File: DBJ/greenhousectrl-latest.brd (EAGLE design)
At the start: 69.5 x 80 mm, 54 parts, among them IC1 ATMEGA168TQFP-08, IC4 L298, J1 5.5x2.1mm Barrel, K1 RELAYPTH4, Q1 MMBT2222A, U2 V_REG_317SMD, Y2 16MHZ

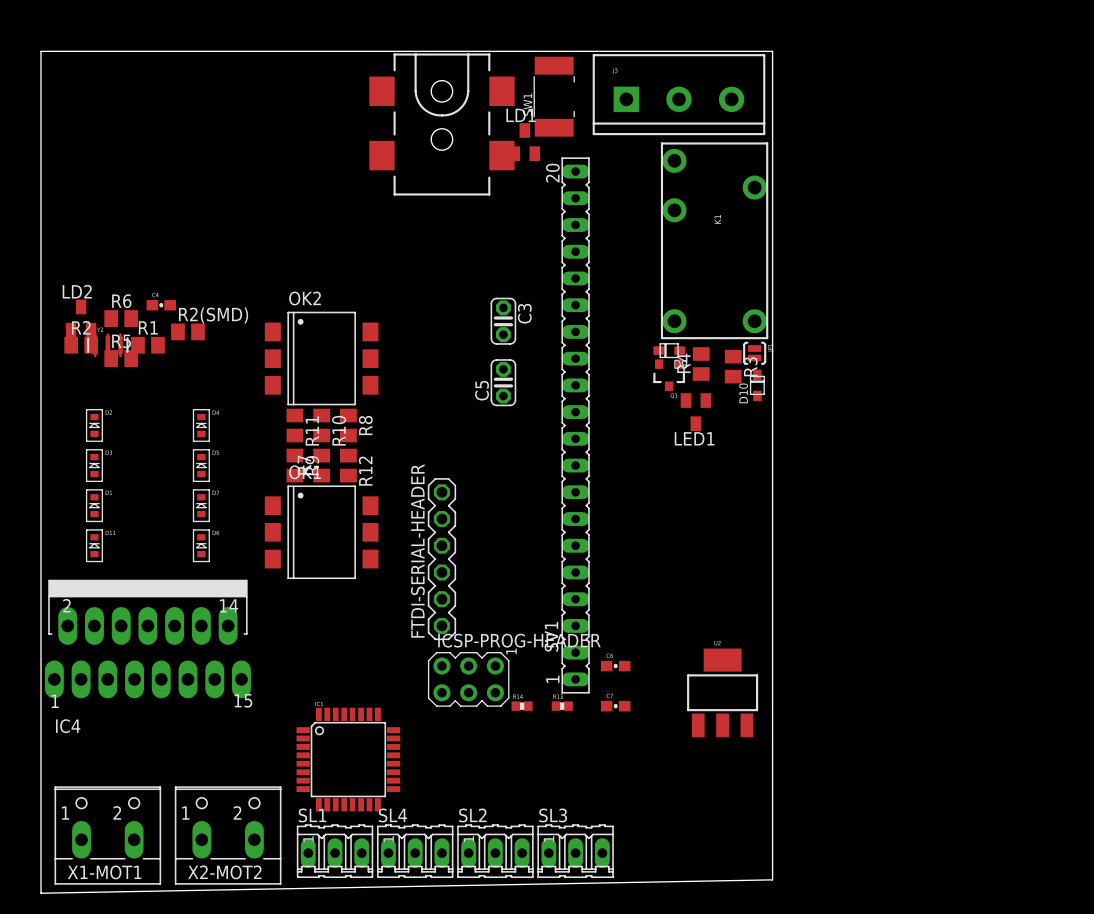
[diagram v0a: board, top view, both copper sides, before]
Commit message: Updated Schematic
clearly shows subsystems for pcb layout
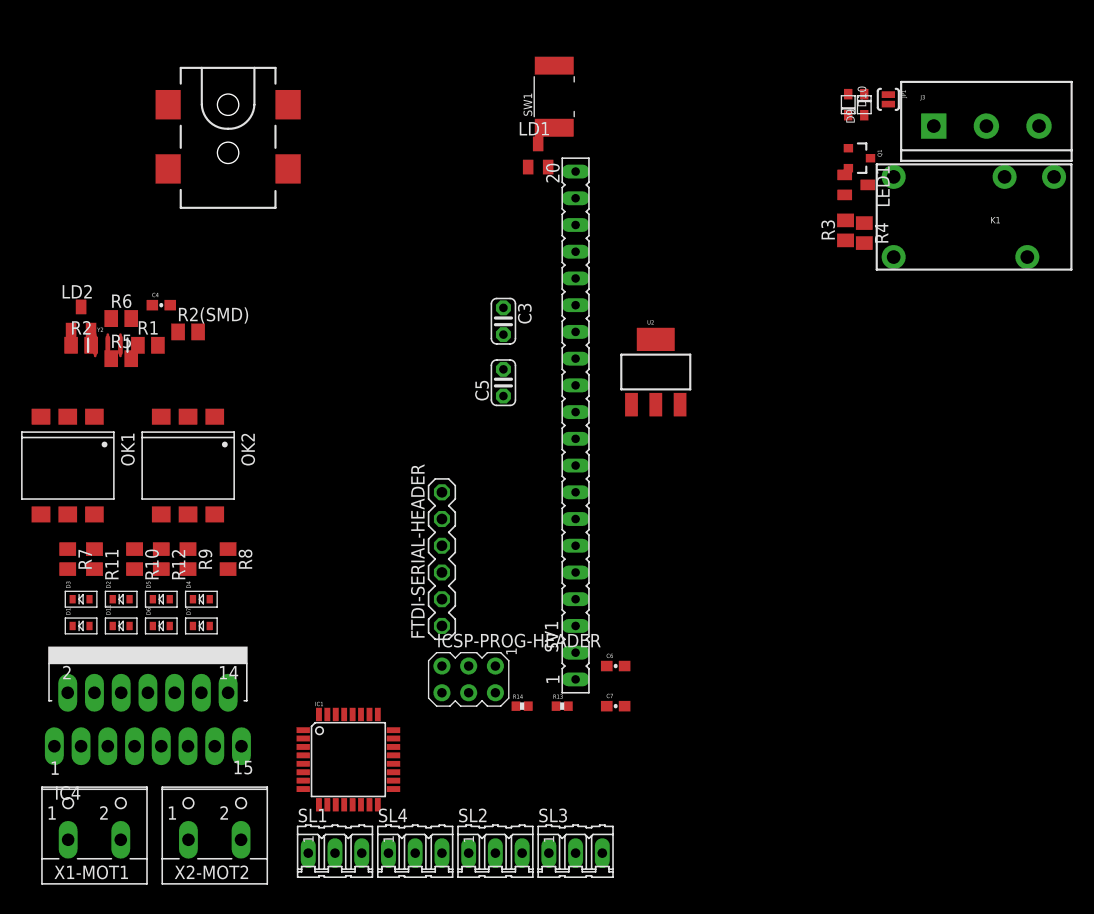
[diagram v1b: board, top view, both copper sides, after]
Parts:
- moved U2 31.1 mm to (58.4, 49.5)
- moved D9 29.8 mm to (78.2, 74.9), turned to 90 degrees
- moved J3 29.3 mm to (84.8, 72.9)
- moved D10 28.0 mm to (76.7, 74.9), turned to 270 degrees
- moved Q1 27.4 mm to (77.7, 69.8), turned to 270 degrees
- moved JP1 27.3 mm to (80.5, 75.4)
- moved LED1 26.4 mm to (77.5, 67.3), turned to 270 degrees
- moved K1 25.9 mm to (89.9, 64.3), turned to 270 degrees
- moved R7 25.7 mm to (2.54, 31.8), turned to 270 degrees
- moved OK1 25.0 mm to (2.54, 40.6), turned to 180 degrees
- moved R11 22.9 mm to (5.08, 31.8)
- moved R10 21.8 mm to (8.89, 31.8)
- moved J1 20.4 mm to (17.8, 74.9)
- moved R12 19.9 mm to (11.4, 31.8)
- moved R4 19.9 mm to (78.2, 62.7), turned to 270 degrees
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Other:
- board outline removed

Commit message: In Lab changes
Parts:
- moved IC4 60.1 mm to (24.1, 80.0)
- moved R3 56.9 mm to (19.6, 62.5), turned to 180 degrees
- moved Q1 55.1 mm to (23.1, 62.2)
- moved R13 52.1 mm to (49.5, 69.8), turned to 270 degrees
- moved C6 50.9 mm to (50.8, 72.4), turned to 270 degrees
- moved C7 50.9 mm to (50.8, 68.6), turned to 90 degrees
- moved LD1 49.9 mm to (2.59, 47.7), turned to 90 degrees
- moved K1 49.8 mm to (40.1, 62.5), turned to 180 degrees
- moved R14 49.7 mm to (49.5, 67.3), turned to 270 degrees
- moved D7 47.0 mm to (30.5, 69.8)
- moved D1 46.6 mm to (17.8, 69.8), turned to 270 degrees
- moved SW1 45.7 mm to (4.32, 65.3), turned to 180 degrees
- moved D3 45.5 mm to (21.6, 69.8), turned to 270 degrees
- moved D4 43.1 mm to (25.4, 69.8), turned to 270 degrees
- moved D6 42.6 mm to (24.1, 66.0), turned to 180 degrees
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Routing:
- net SEN_B: track 0.00 -> 26.6 mm, vias 0 -> 2
- net NO: track 0.00 -> 25.1 mm
- net COIL: track 0.00 -> 24.3 mm, vias 0 -> 1
- net NC: track 0.00 -> 23.2 mm
- net COMMON: track 0.00 -> 22.4 mm
- net +5V: track 0.00 -> 20.3 mm
- net GND: track 0.00 -> 20.2 mm
- net TX: track 0.00 -> 18.5 mm, vias 0 -> 2
- net MISO: track 0.00 -> 14.2 mm, vias 0 -> 2
- net SCK: track 0.00 -> 13.5 mm, vias 0 -> 2
- net MOSI: track 0.00 -> 12.6 mm
- net +12V: track 0.00 -> 8.64 mm
- net VCC: track 0.00 -> 7.04 mm
- net SEN_A: track 0.00 -> 6.80 mm
- net DIODENODE: track 0.00 -> 6.04 mm
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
